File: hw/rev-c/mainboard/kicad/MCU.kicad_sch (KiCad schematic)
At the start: 34 parts, among them J25 MENU, SW4 RUN, SW5 MENU, U21 RP2040, Y1 12 MHz

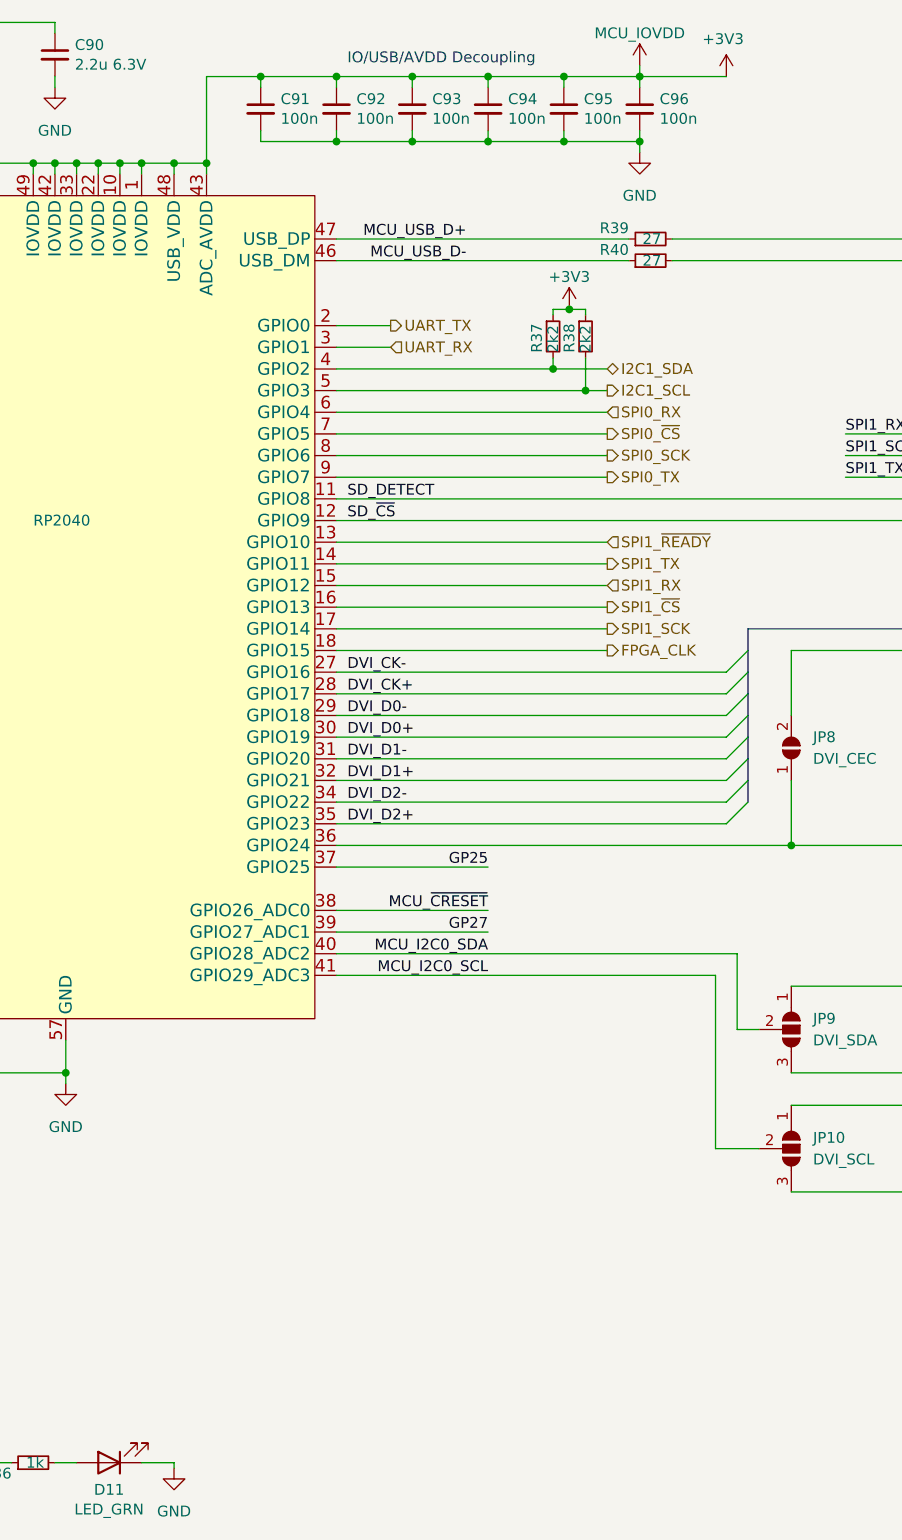
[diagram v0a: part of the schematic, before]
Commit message: hw: fix wire/grid violations in schematic
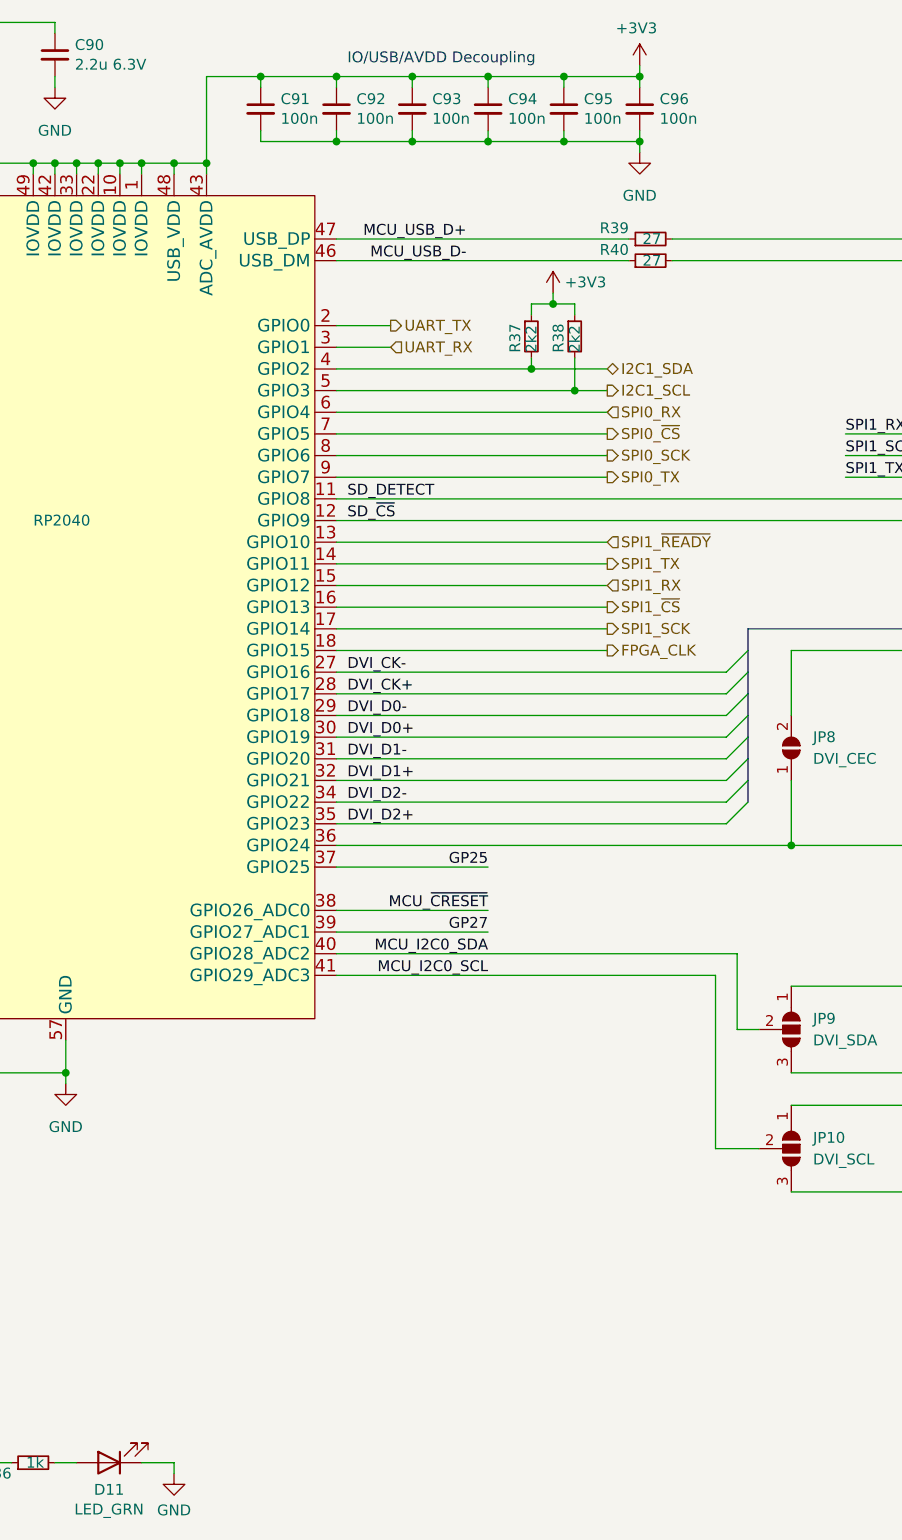
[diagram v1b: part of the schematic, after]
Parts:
- U21: symbol Retrocomputing:RP2040 -> EconoPET:RP2040
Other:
- moved on the sheet: R37, R38

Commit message: hw: update diode and connector symbols
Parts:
- J25: symbol Connector:Conn_01x02_Male -> Connector:Conn_01x02_Pin
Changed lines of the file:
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@@
 	)
 	(symbol
-		(lib_id "Connector:Conn_01x02_Male")
+		(lib_id "Connector:Conn_01x02_Pin")
 		(at 25.4 168.91 0)
 		(mirror x)
@@
 			)
 		)
-		(property "Description" ""
+		(property "Description" "Generic connector, single row, 01x02, script generated"
 			(at 25.4 168.91 0)
 			(effects

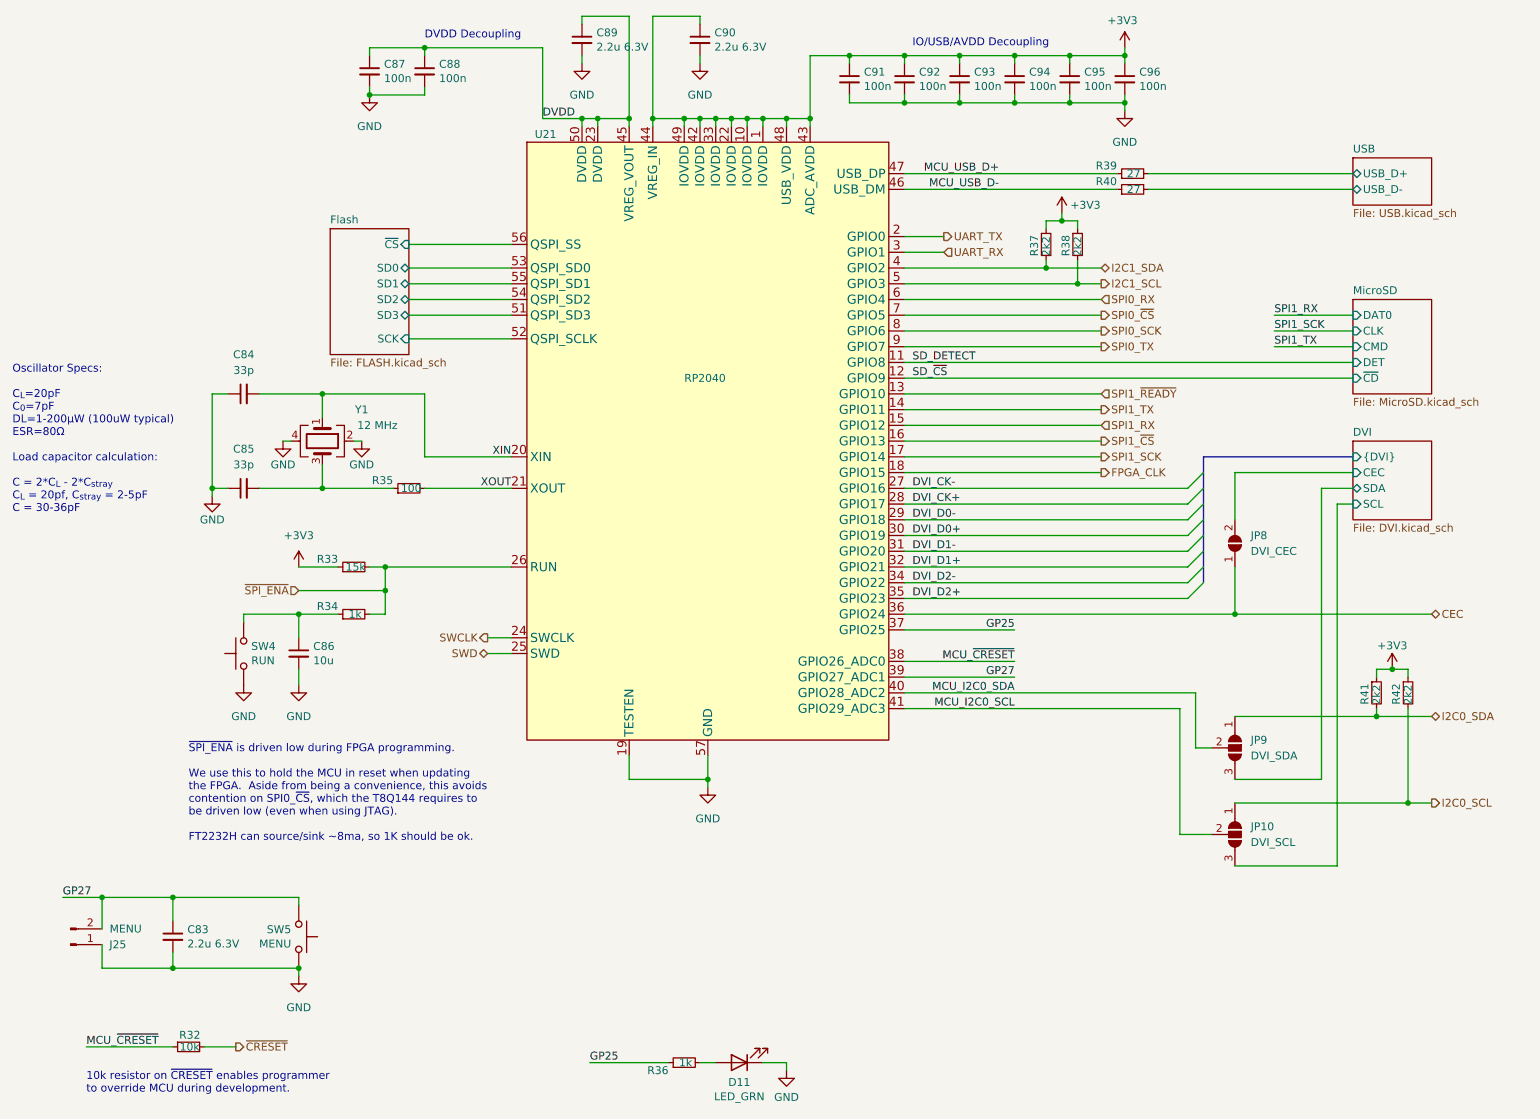
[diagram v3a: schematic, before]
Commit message: hw: renumber reference designators
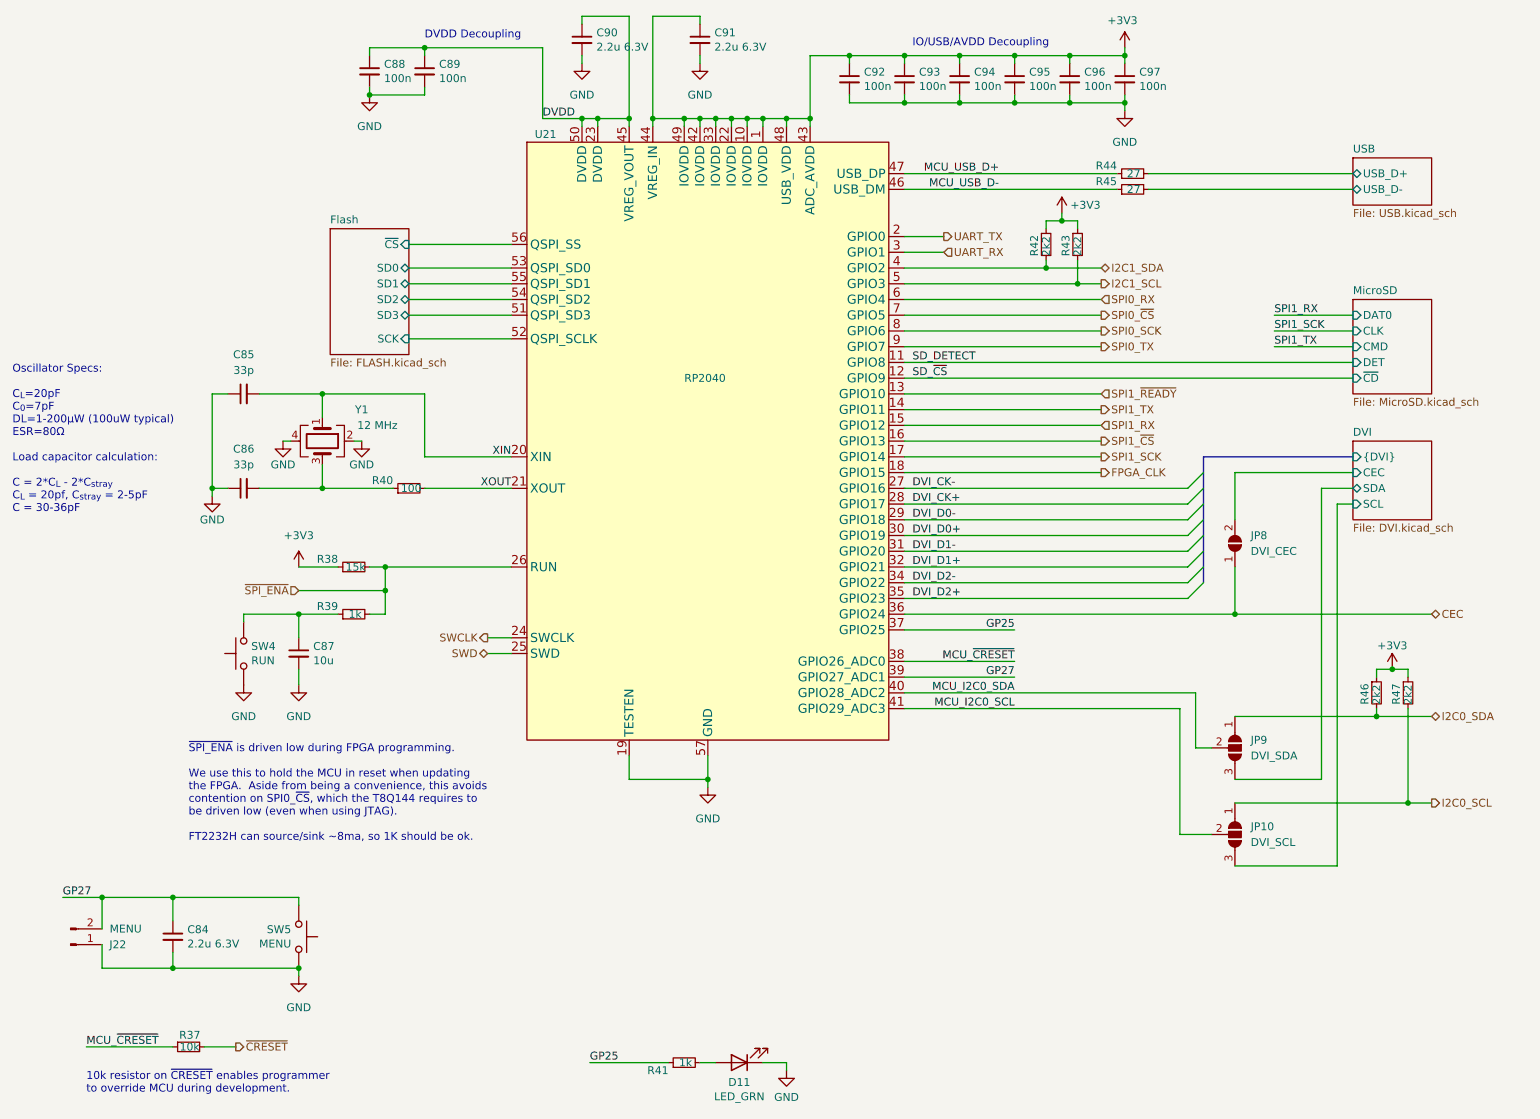
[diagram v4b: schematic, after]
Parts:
- renumbered C83 to C84, C84 to C85, C85 to C86, C86 to C87, C87 to C88, C88 to C89, C89 to C90, C90 to C91, C91 to C92, C92 to C93, C93 to C94, C94 to C95, C95 to C96, C96 to C97, J25 to J22, R32 to R37, R33 to R38, R34 to R39, R35 to R40, R36 to R41, R37 to R42, R38 to R43, R39 to R44, R40 to R45, R41 to R46, R42 to R47

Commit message: hw: match original PET designators for connectors
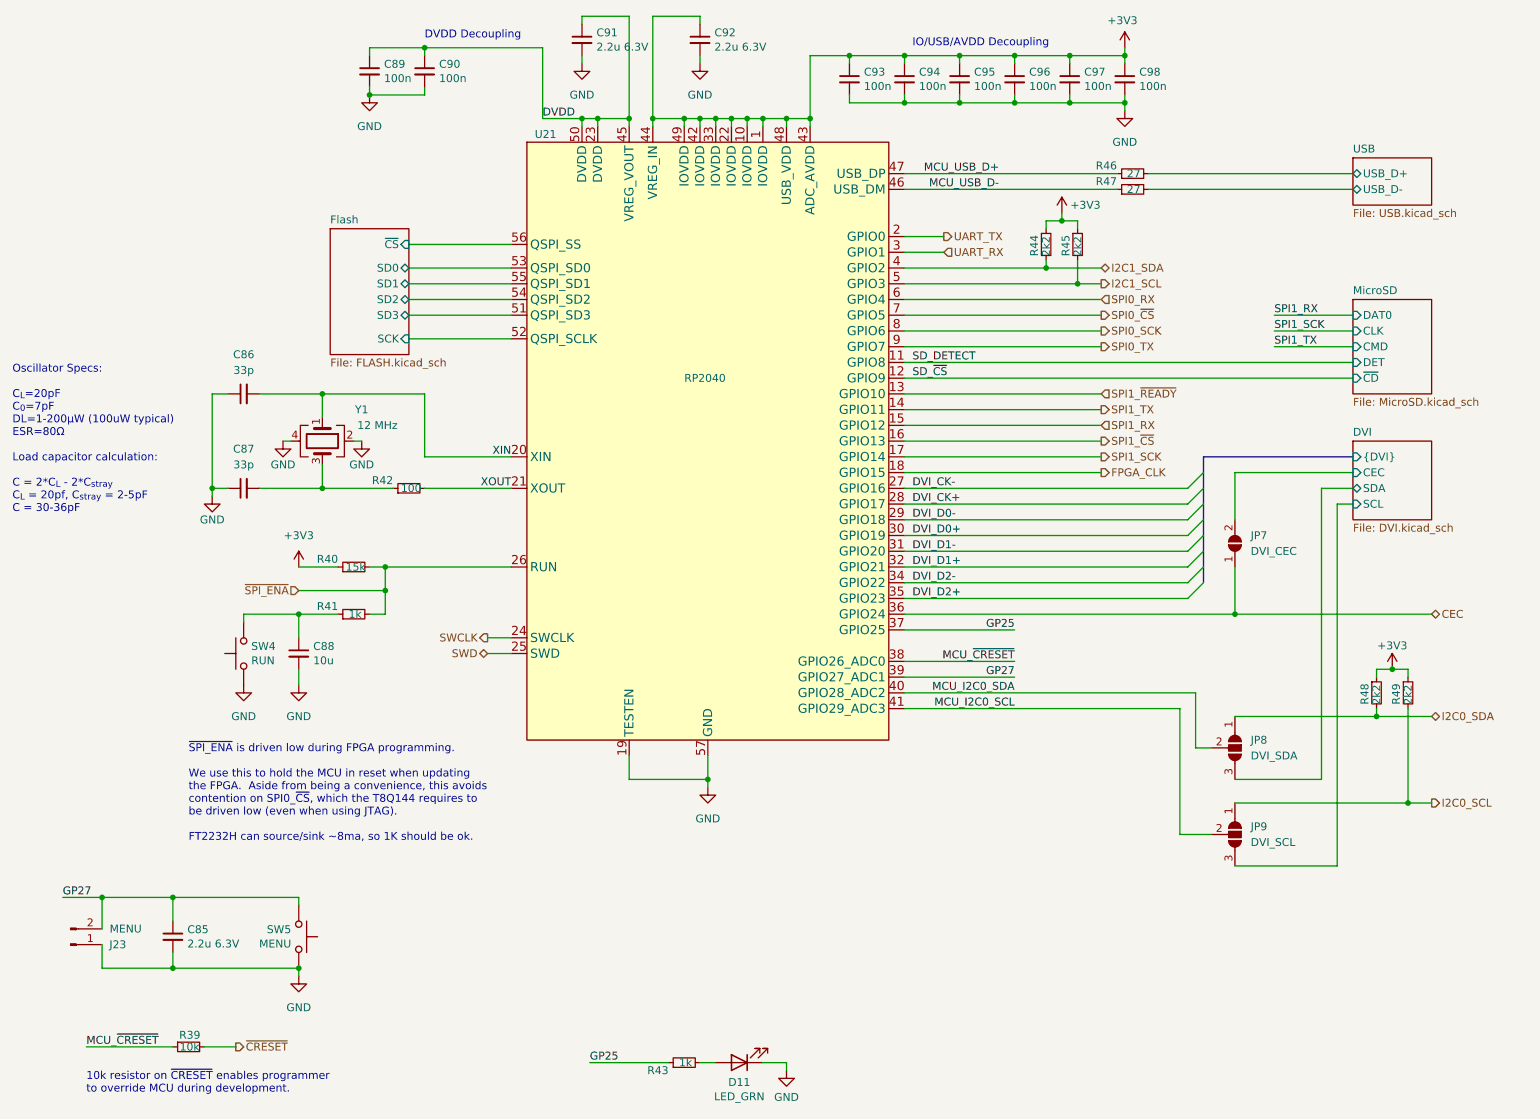
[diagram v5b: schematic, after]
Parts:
- renumbered C84 to C85, C85 to C86, C86 to C87, C87 to C88, C88 to C89, C89 to C90, C90 to C91, C91 to C92, C92 to C93, C93 to C94, C94 to C95, C95 to C96, C96 to C97, C97 to C98, J22 to J23, JP8 to JP7, JP9 to JP8, JP10 to JP9, R37 to R39, R38 to R40, R39 to R41, R40 to R42, R41 to R43, R42 to R44, R43 to R45, R44 to R46, R45 to R47, R46 to R48, R47 to R49

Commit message: hw: tidy warnings
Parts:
- C88: value 10u -> 4.7u 10V; footprint Capacitor_SMD:C_0603_1608Metric -> Capacitor_SMD:C_0402_1005Metric; LCSC C96446 -> C23733
- SW4: footprint JLCPCB:SW-TH_L6.0-W3.5-P6.50 -> EconoPET:SW_PUSH_1P1T_6x3.5mm_H4.3_APEM_MJTP1243
- renumbered C89 to C3
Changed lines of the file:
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@@
 			)
 		)
-		(property "Footprint" "JLCPCB:SW-TH_L6.0-W3.5-P6.50"
+		(property "Footprint" "EconoPET:SW_PUSH_1P1T_6x3.5mm_H4.3_APEM_MJTP1243"
 			(at 48.26 121.92 0)
 			(effects
@@
 	)
 	(symbol
-		(lib_id "Device:C_Small")
-		(at 62.23 121.92 0)
-		(unit 1)
-		(exclude_from_sim no)
-		(in_bom yes)
-		(on_board yes)
-		(dnp no)
-		(property "Reference" "C88"
-			(at 64.5668 120.7516 0)
-			(effects
-				(font
-					(size 1.27 1.27)
-				)
-				(justify left)
-			)
-		)
-		(property "Value" "10u"
-			(at 64.5668 123.063 0)
-			(effects
-				(font
-					(size 1.27 1.27)
-				)
-				(justify left)
-			)
-		)
-		(property "Footprint" "Capacitor_SMD:C_0603_1608Metric"
-			(at 62.23 121.92 0)
-			(effects
-				(font
-					(size 1.27 1.27)
-				)
-				(hide yes)
-			)
-		)
-		(property "Datasheet" "https://product.samsungsem.com/mlcc/CL10A106MA8NRN.do"
-			(at 62.23 121.92 0)
-			(effects
-				(font
-					(size 1.27 1.27)
-				)
-				(hide yes)
-			)
-		)
-		(property "Description" ""
-			(at 62.23 121.92 0)
-			(effects
-				(font
-					(size 1.27 1.27)
-				)
-				(hide yes)
-			)
-		)
-		(property "LCSC" "C96446"
-			(at 62.23 121.92 0)
-			(effects
-				(font
-					(size 1.27 1.27)
-				)
-				(hide yes)
-			)
-		)
-		(pin "1"
-		)
-		(pin "2"
-		)
-		(instances
-			(project ""
-				(path "/2eea20e6-112c-411a-b615-885ae773135a/00000000-0000-0000-0000-0000617d6918/b70241ab-8a5c-42d5-a1ab-8f4bc50a1197"
-					(reference "C88")
-					(unit 1)
-				)
-			)
-		)
-	)
-	(symbol
 		(lib_id "Device:R_Small")
 		(at 80.01 95.25 90)
@@
 	)
 	(symbol
+		(lib_id "Device:C_Small")
+		(at 62.23 121.92 0)
+		(unit 1)
+		(exclude_from_sim no)
+		(in_bom yes)
+		(on_board yes)
+		(dnp no)
+		(property "Reference" "C88"
+			(at 64.5668 120.7516 0)
+			(effects
+				(font
+					(size 1.27 1.27)
+				)
+				(justify left)
+			)
+		)
+		(property "Value" "4.7u 10V"
+			(at 64.5668 123.063 0)
+			(effects
+				(font
+					(size 1.27 1.27)
+				)
+				(justify left)
+			)
+		)
+		(property "Footprint" "Capacitor_SMD:C_0402_1005Metric"
+			(at 62.23 121.92 0)
+			(effects
+				(font
+					(size 1.27 1.27)
+				)
+				(hide yes)
+			)
+		)
+		(property "Datasheet" "https://product.samsungsem.com/mlcc/CL05A475MP5NRN.do"
+			(at 62.23 121.92 0)
+			(effects
+				(font
+					(size 1.27 1.27)
+				)
+				(hide yes)
+			)
+		)
+		(property "Description" ""
+			(at 62.23 121.92 0)
+			(effects
+				(font
+					(size 1.27 1.27)
+				)
+				(hide yes)
+			)
+		)
+		(property "LCSC" "C23733"
+			(at 62.23 121.92 0)
+			(effects
+				(font
+					(size 1.27 1.27)
+				)
+				(hide yes)
+			)
+		)
+		(pin "1"
+		)
+		(pin "2"
+		)
+		(instances
+			(project "Mainboard"
+				(path "/2eea20e6-112c-411a-b615-885ae773135a/00000000-0000-0000-0000-0000617d6918/b70241ab-8a5c-42d5-a1ab-8f4bc50a1197"
+					(reference "C88")
+					(unit 1)
+				)
+			)
+		)
+	)
+	(symbol
 		(lib_id "power:GND")
 		(at 140.97 189.23 0)
@@
 		(on_board yes)
 		(dnp no)
-		(property "Reference" "C89"
+		(property "Reference" "C3"
 			(at 75.9968 26.7716 0)
 			(effects
@@
 			(project ""
 				(path "/2eea20e6-112c-411a-b615-885ae773135a/00000000-0000-0000-0000-0000617d6918/b70241ab-8a5c-42d5-a1ab-8f4bc50a1197"
-					(reference "C89")
-					(unit 1)
-				)
+					(reference "C3")
+					(unit 1)
+				)
